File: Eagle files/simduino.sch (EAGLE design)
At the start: 15 parts, among them IC1 ATMEGA168-20P, Q1 16MHz

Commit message: Streamlining
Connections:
- net +5USB: now also C5.1; no longer C5.2
- net GND: now also C5.2; no longer C5.1
- net N$2: now also S1.P
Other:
- moved on the sheet: C5, R4
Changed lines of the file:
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@@
 </instance>
 <instance part="C2" gate="G$1" x="2.54" y="22.86"/>
-<instance part="R4" gate="G$1" x="15.24" y="17.78" smashed="yes" rot="R270">
-<attribute name="NAME" x="16.9926" y="17.526" size="1.778" layer="95" rot="R270"/>
-<attribute name="VALUE" x="16.764" y="22.352" size="1.778" layer="96" rot="R270"/>
+<instance part="R4" gate="G$1" x="17.78" y="17.78" smashed="yes" rot="R270">
+<attribute name="NAME" x="19.5326" y="17.526" size="1.778" layer="95" rot="R270"/>
+<attribute name="VALUE" x="19.304" y="22.352" size="1.778" layer="96" rot="R270"/>
 </instance>
 <instance part="Q1" gate="G$1" x="38.1" y="63.5" smashed="yes" rot="R90">
@@
 </instance>
 <instance part="GND8" gate="1" x="27.94" y="38.1"/>
-<instance part="C5" gate="G$1" x="33.02" y="43.18" smashed="yes" rot="R90">
-<attribute name="NAME" x="32.766" y="45.847" size="1.778" layer="95" rot="R180"/>
-<attribute name="VALUE" x="40.386" y="42.291" size="1.778" layer="96" rot="R180"/>
+<instance part="C5" gate="G$1" x="10.16" y="22.86" smashed="yes">
+<attribute name="NAME" x="12.827" y="23.114" size="1.778" layer="95" rot="R90"/>
+<attribute name="VALUE" x="9.271" y="15.494" size="1.778" layer="96" rot="R90"/>
 </instance>
 <instance part="GND7" gate="1" x="2.54" y="12.7"/>
@@
 </segment>
 <segment>
-<wire x1="27.94" y1="40.64" x2="27.94" y2="43.18" width="0.1524" layer="91"/>
-<wire x1="27.94" y1="43.18" x2="27.94" y2="53.34" width="0.1524" layer="91"/>
+<wire x1="27.94" y1="40.64" x2="27.94" y2="53.34" width="0.1524" layer="91"/>
 <wire x1="27.94" y1="53.34" x2="27.94" y2="60.96" width="0.1524" layer="91"/>
 <wire x1="27.94" y1="60.96" x2="27.94" y2="66.04" width="0.1524" layer="91"/>
@@
 <wire x1="27.94" y1="78.74" x2="40.64" y2="78.74" width="0.1524" layer="91"/>
 <wire x1="40.64" y1="53.34" x2="27.94" y2="53.34" width="0.1524" layer="91"/>
-<wire x1="30.48" y1="43.18" x2="27.94" y2="43.18" width="0.1524" layer="91"/>
 <wire x1="27.94" y1="86.36" x2="27.94" y2="83.82" width="0.1524" layer="91"/>
 <wire x1="27.94" y1="83.82" x2="27.94" y2="78.74" width="0.1524" layer="91"/>
@@
 <junction x="27.94" y="66.04"/>
 <junction x="27.94" y="53.34"/>
-<junction x="27.94" y="43.18"/>
 <junction x="27.94" y="78.74"/>
 <junction x="27.94" y="83.82"/>
@@
 <pinref part="IC1" gate="G$1" pin="AGND"/>
 <pinref part="IC1" gate="G$1" pin="GND"/>
-<pinref part="C5" gate="G$1" pin="1"/>
 <pinref part="S1" gate="1" pin="S"/>
 <pinref part="S1" gate="1" pin="S1"/>
@@
 <pinref part="GND7" gate="1" pin="GND"/>
 <pinref part="C2" gate="G$1" pin="-"/>
+<pinref part="C5" gate="G$1" pin="2"/>
+<wire x1="10.16" y1="17.78" x2="2.54" y2="17.78" width="0.1524" layer="91"/>
 </segment>
 <segment>
@@
 <wire x1="-2.54" y1="12.7" x2="-2.54" y2="27.94" width="0.1524" layer="91"/>
 <pinref part="X1" gate="G$1" pin="1"/>
-<wire x1="38.1" y1="48.26" x2="40.64" y2="48.26" width="0.1524" layer="91"/>
-<wire x1="38.1" y1="43.18" x2="38.1" y2="48.26" width="0.1524" layer="91"/>
-<wire x1="17.78" y1="48.26" x2="38.1" y2="48.26" width="0.1524" layer="91"/>
+<wire x1="17.78" y1="48.26" x2="40.64" y2="48.26" width="0.1524" layer="91"/>
 <wire x1="40.64" y1="73.66" x2="17.78" y2="73.66" width="0.1524" layer="91"/>
 <wire x1="17.78" y1="73.66" x2="17.78" y2="48.26" width="0.1524" layer="91"/>
-<wire x1="15.24" y1="27.94" x2="15.24" y2="22.86" width="0.1524" layer="91"/>
-<wire x1="15.24" y1="27.94" x2="17.78" y2="27.94" width="0.1524" layer="91"/>
 <wire x1="17.78" y1="27.94" x2="17.78" y2="48.26" width="0.1524" layer="91"/>
-<wire x1="2.54" y1="27.94" x2="15.24" y2="27.94" width="0.1524" layer="91"/>
+<wire x1="2.54" y1="27.94" x2="10.16" y2="27.94" width="0.1524" layer="91"/>
+<wire x1="10.16" y1="27.94" x2="17.78" y2="27.94" width="0.1524" layer="91"/>
 <wire x1="2.54" y1="25.4" x2="2.54" y2="27.94" width="0.1524" layer="91"/>
 <wire x1="-2.54" y1="27.94" x2="2.54" y2="27.94" width="0.1524" layer="91"/>
-<junction x="38.1" y="48.26"/>
 <junction x="17.78" y="48.26"/>
-<junction x="15.24" y="27.94"/>
 <junction x="2.54" y="27.94"/>
 <pinref part="IC1" gate="G$1" pin="VCC"/>
-<pinref part="C5" gate="G$1" pin="2"/>
 <pinref part="IC1" gate="G$1" pin="AVCC"/>
+<pinref part="C2" gate="G$1" pin="+"/>
+<pinref part="C5" gate="G$1" pin="1"/>
+<wire x1="10.16" y1="25.4" x2="10.16" y2="27.94" width="0.1524" layer="91"/>
 <pinref part="R4" gate="G$1" pin="1"/>
-<pinref part="C2" gate="G$1" pin="+"/>
+<wire x1="17.78" y1="22.86" x2="17.78" y2="27.94" width="0.1524" layer="91"/>
 </segment>
 </net>
@@
 <pinref part="IC1" gate="G$1" pin="PC6(/RESET/PCI14)"/>
 <pinref part="S1" gate="1" pin="P1"/>
+<pinref part="S1" gate="1" pin="P"/>
+<wire x1="38.1" y1="83.82" x2="38.1" y2="86.36" width="0.1524" layer="91"/>
 </segment>
 </net>
@@
 <segment>
 <wire x1="-5.08" y1="10.16" x2="2.54" y2="10.16" width="0.1524" layer="91"/>
-<wire x1="2.54" y1="10.16" x2="15.24" y2="10.16" width="0.1524" layer="91"/>
-<wire x1="15.24" y1="10.16" x2="40.64" y2="10.16" width="0.1524" layer="91"/>
+<wire x1="2.54" y1="10.16" x2="17.78" y2="10.16" width="0.1524" layer="91"/>
+<wire x1="17.78" y1="10.16" x2="40.64" y2="10.16" width="0.1524" layer="91"/>
 <wire x1="2.54" y1="5.08" x2="2.54" y2="10.16" width="0.1524" layer="91"/>
-<wire x1="15.24" y1="12.7" x2="15.24" y2="10.16" width="0.1524" layer="91"/>
 <junction x="2.54" y="10.16"/>
-<junction x="15.24" y="10.16"/>
 <label x="21.082" y="10.414" size="1.778" layer="95"/>
 <pinref part="X1" gate="G$1" pin="2"/>
@@
 <pinref part="D1" gate="G$1" pin="C"/>
 <pinref part="R4" gate="G$1" pin="2"/>
+<wire x1="17.78" y1="12.7" x2="17.78" y2="10.16" width="0.1524" layer="91"/>
 </segment>
 </net>

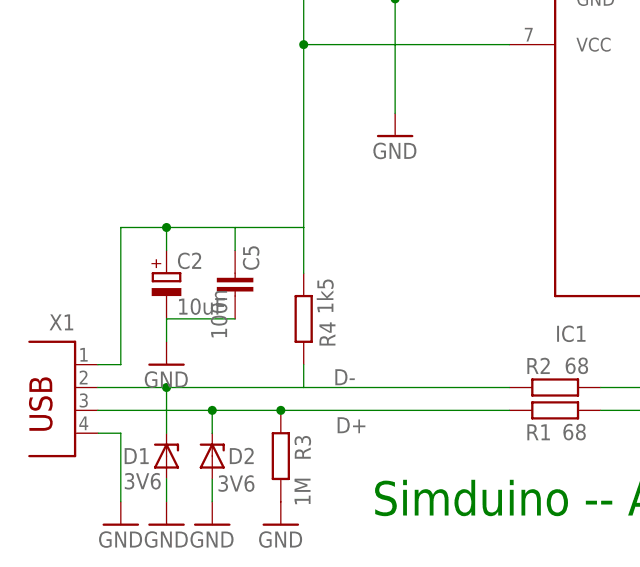
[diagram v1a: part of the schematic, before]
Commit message: Rerouting
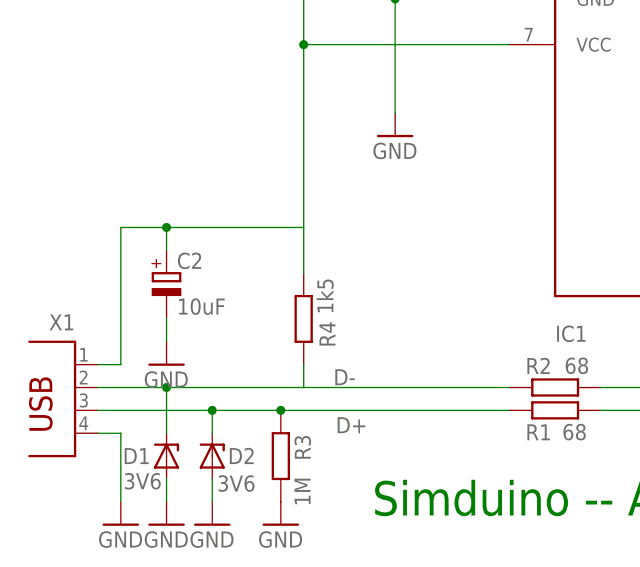
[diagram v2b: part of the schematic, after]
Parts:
- removed C5: 100n, rcl:C-EU025_050-025X075
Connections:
- net +5USB: no longer C5.1
- net GND: no longer C5.2
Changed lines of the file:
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@@
 <part name="C4" library="rcl" deviceset="C-EU" device="025-024X044" value="22p"/>
 <part name="GND8" library="supply1" deviceset="GND" device=""/>
-<part name="C5" library="rcl" deviceset="C-EU" device="025_050-025X075" value="100n"/>
 <part name="GND7" library="supply1" deviceset="GND" device=""/>
 <part name="GND9" library="supply1" deviceset="GND" device=""/>
@@
 </instance>
 <instance part="GND8" gate="1" x="27.94" y="38.1"/>
-<instance part="C5" gate="G$1" x="10.16" y="22.86" smashed="yes">
-<attribute name="NAME" x="12.827" y="23.114" size="1.778" layer="95" rot="R90"/>
-<attribute name="VALUE" x="9.271" y="15.494" size="1.778" layer="96" rot="R90"/>
-</instance>
 <instance part="GND7" gate="1" x="2.54" y="12.7"/>
 <instance part="GND9" gate="1" x="104.14" y="66.04" rot="R270"/>
@@
 <pinref part="GND7" gate="1" pin="GND"/>
 <pinref part="C2" gate="G$1" pin="-"/>
-<pinref part="C5" gate="G$1" pin="2"/>
-<wire x1="10.16" y1="17.78" x2="2.54" y2="17.78" width="0.1524" layer="91"/>
 </segment>
 <segment>
@@
 <wire x1="17.78" y1="73.66" x2="17.78" y2="48.26" width="0.1524" layer="91"/>
 <wire x1="17.78" y1="27.94" x2="17.78" y2="48.26" width="0.1524" layer="91"/>
-<wire x1="2.54" y1="27.94" x2="10.16" y2="27.94" width="0.1524" layer="91"/>
-<wire x1="10.16" y1="27.94" x2="17.78" y2="27.94" width="0.1524" layer="91"/>
+<wire x1="2.54" y1="27.94" x2="17.78" y2="27.94" width="0.1524" layer="91"/>
 <wire x1="2.54" y1="25.4" x2="2.54" y2="27.94" width="0.1524" layer="91"/>
 <wire x1="-2.54" y1="27.94" x2="2.54" y2="27.94" width="0.1524" layer="91"/>
@@
 <pinref part="IC1" gate="G$1" pin="AVCC"/>
 <pinref part="C2" gate="G$1" pin="+"/>
-<pinref part="C5" gate="G$1" pin="1"/>
-<wire x1="10.16" y1="25.4" x2="10.16" y2="27.94" width="0.1524" layer="91"/>
 <pinref part="R4" gate="G$1" pin="1"/>
 <wire x1="17.78" y1="22.86" x2="17.78" y2="27.94" width="0.1524" layer="91"/>
